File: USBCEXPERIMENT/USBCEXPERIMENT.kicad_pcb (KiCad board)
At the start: 2 copper layers, 7.8 x 4.5 mm, 3 parts, among them J1 USB_C_Receptacle, J2 Conn_01x10_Male, J3 Conn_01x10_Male

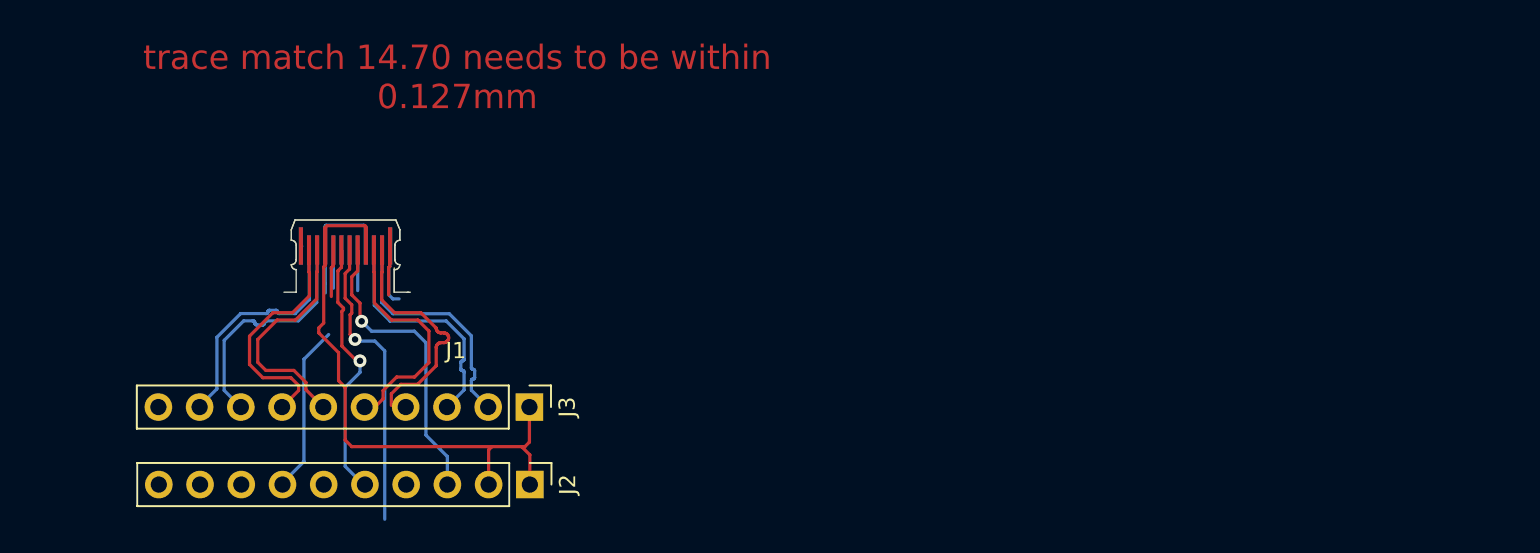
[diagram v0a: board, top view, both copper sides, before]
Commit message: started to add a simple version to the PCB
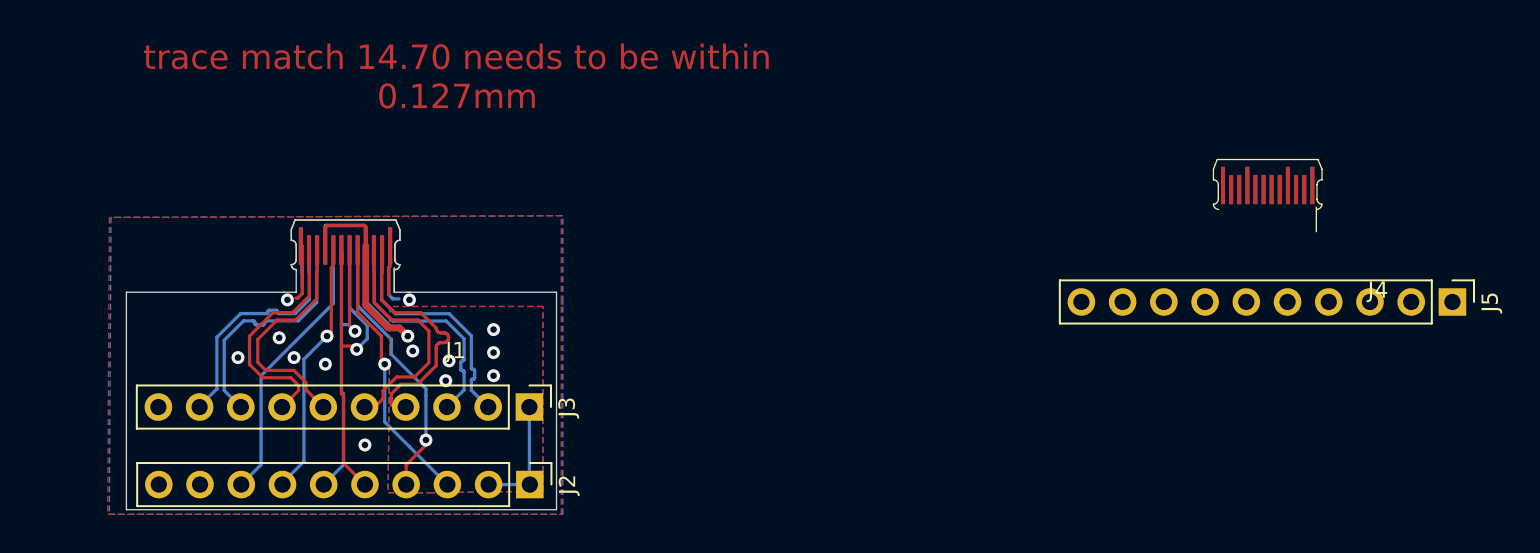
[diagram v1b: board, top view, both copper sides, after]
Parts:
- added J4: USB_C_Receptacle, footprint:usb-c-pcb, F.Cu at (207.8, 89.3)
- added J5: Conn_01x10_Male, Connector_PinHeader_2.54mm:PinHeader_1x10_P2.54mm_Vertical, F.Cu at (219.2, 93.6)
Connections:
- J2 pad 4: /CC2 -> /SBUS2
- J2 pad 8: /SBUS2 -> /CC2
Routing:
- net /CC2: track 2.35 -> 16.8 mm
- net /SBUS2: track 2.50 -> 16.7 mm, vias 0 -> 1
- net VBUS: track 44.3 -> 31.5 mm, vias 0 -> 7
- net /USBD-: track 16.3 -> 22.9 mm
- net GND: track 6.85 -> 13.3 mm, vias 0 -> 7
- net /USBD+: track 18.4 -> 21.2 mm
- net /SBUS1: track 13.3 -> 15.9 mm, vias 0 -> 1
- net /CC1: track 18.6 -> 16.7 mm
- net /TX1+: track 14.7 -> 15.7 mm
- added copper zone on B.Cu, net GND
- added copper zone on F.Cu, net GND
- added copper zone on B.Cu, net VBUS
- added copper zone on F.Cu, net VBUS
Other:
- board size 7.8 x 4.5 mm -> 26.5 x 17.9 mm
